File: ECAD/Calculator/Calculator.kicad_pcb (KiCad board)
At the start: 2 copper layers, 26 x 49 mm, 30 parts, among them SW1 Switch_Tactile_ESwitch, SW10 Switch_Tactile_ESwitch, SW11 Switch_Tactile_ESwitch, SW12 Switch_Tactile_ESwitch, SW13 Switch_Tactile_ESwitch, SW14 Switch_Tactile_ESwitch, SW15 Switch_Tactile_ESwitch, SW16 Switch_Tactile_ESwitch, SW17 Switch_Tactile_ESwitch, SW18 Switch_Tactile_ESwitch, SW19 Switch_Tactile_ESwitch, SW2 Switch_Tactile_ESwitch, SW20 Switch_Tactile_ESwitch, SW3 Switch_Tactile_ESwitch, SW4 Switch_Tactile_ESwitch, SW5 Switch_Tactile_ESwitch, SW6 Switch_Tactile_ESwitch, SW7 Switch_Tactile_ESwitch, SW8 Switch_Tactile_ESwitch, SW9 Switch_Tactile_ESwitch

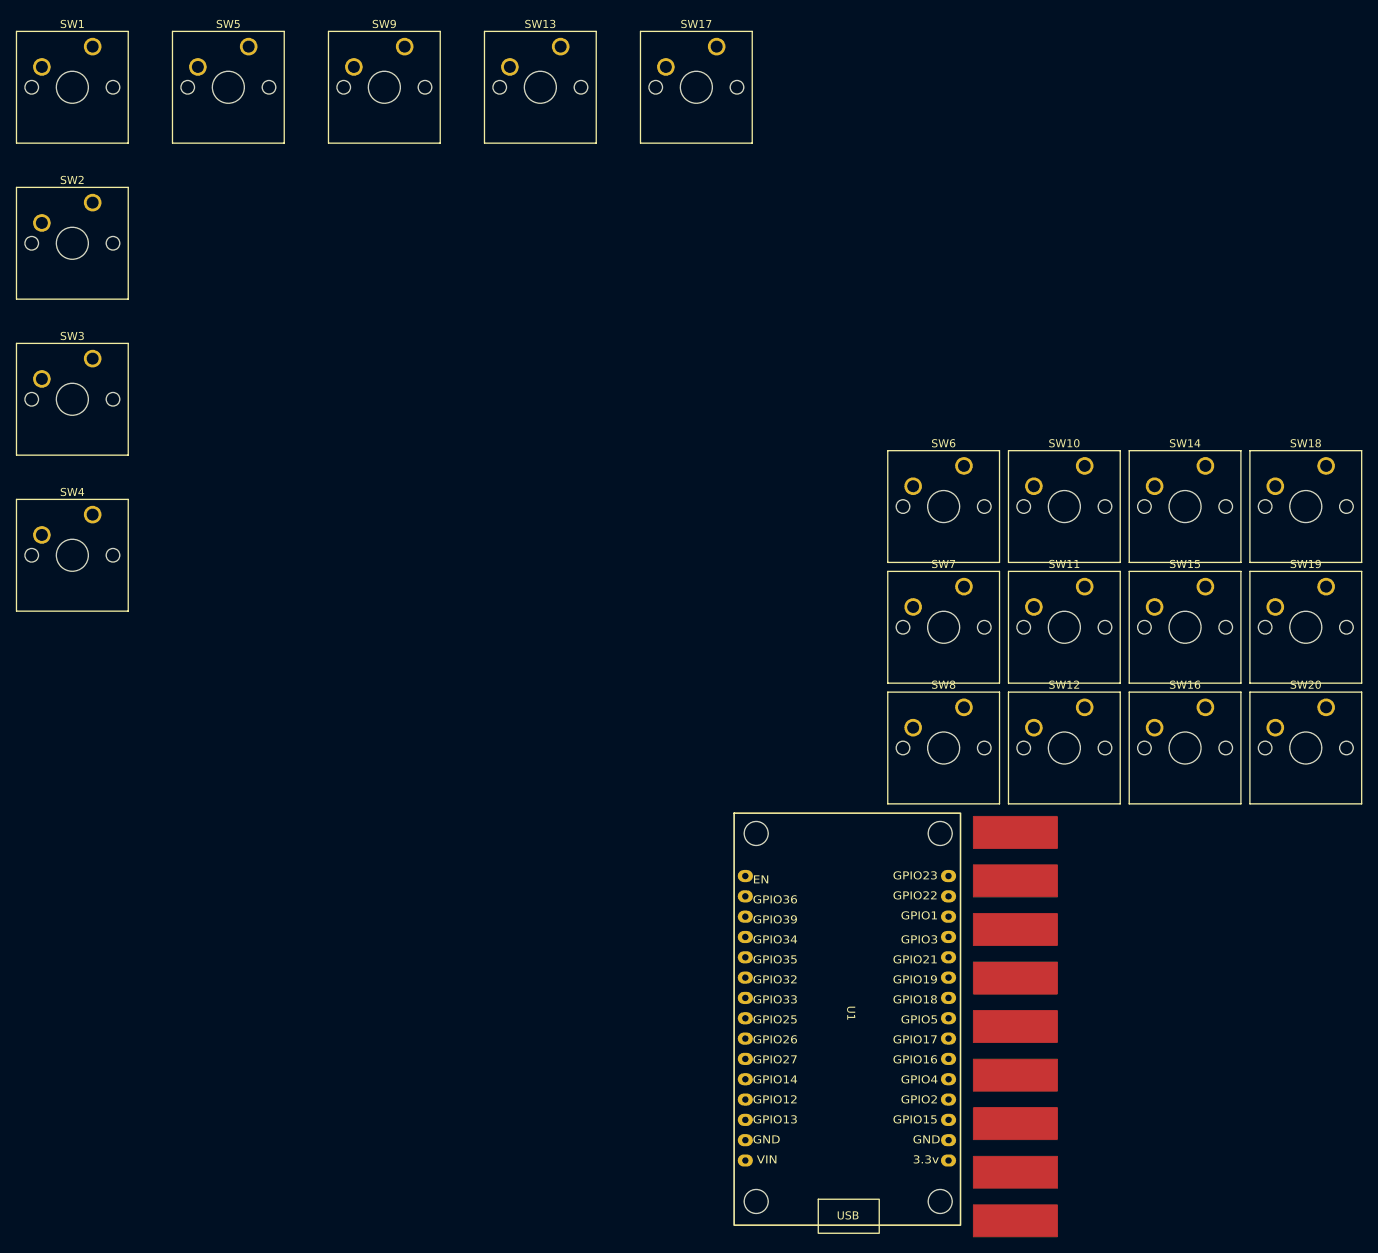
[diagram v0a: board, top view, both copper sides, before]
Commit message: Completed layout for footprints for PCB
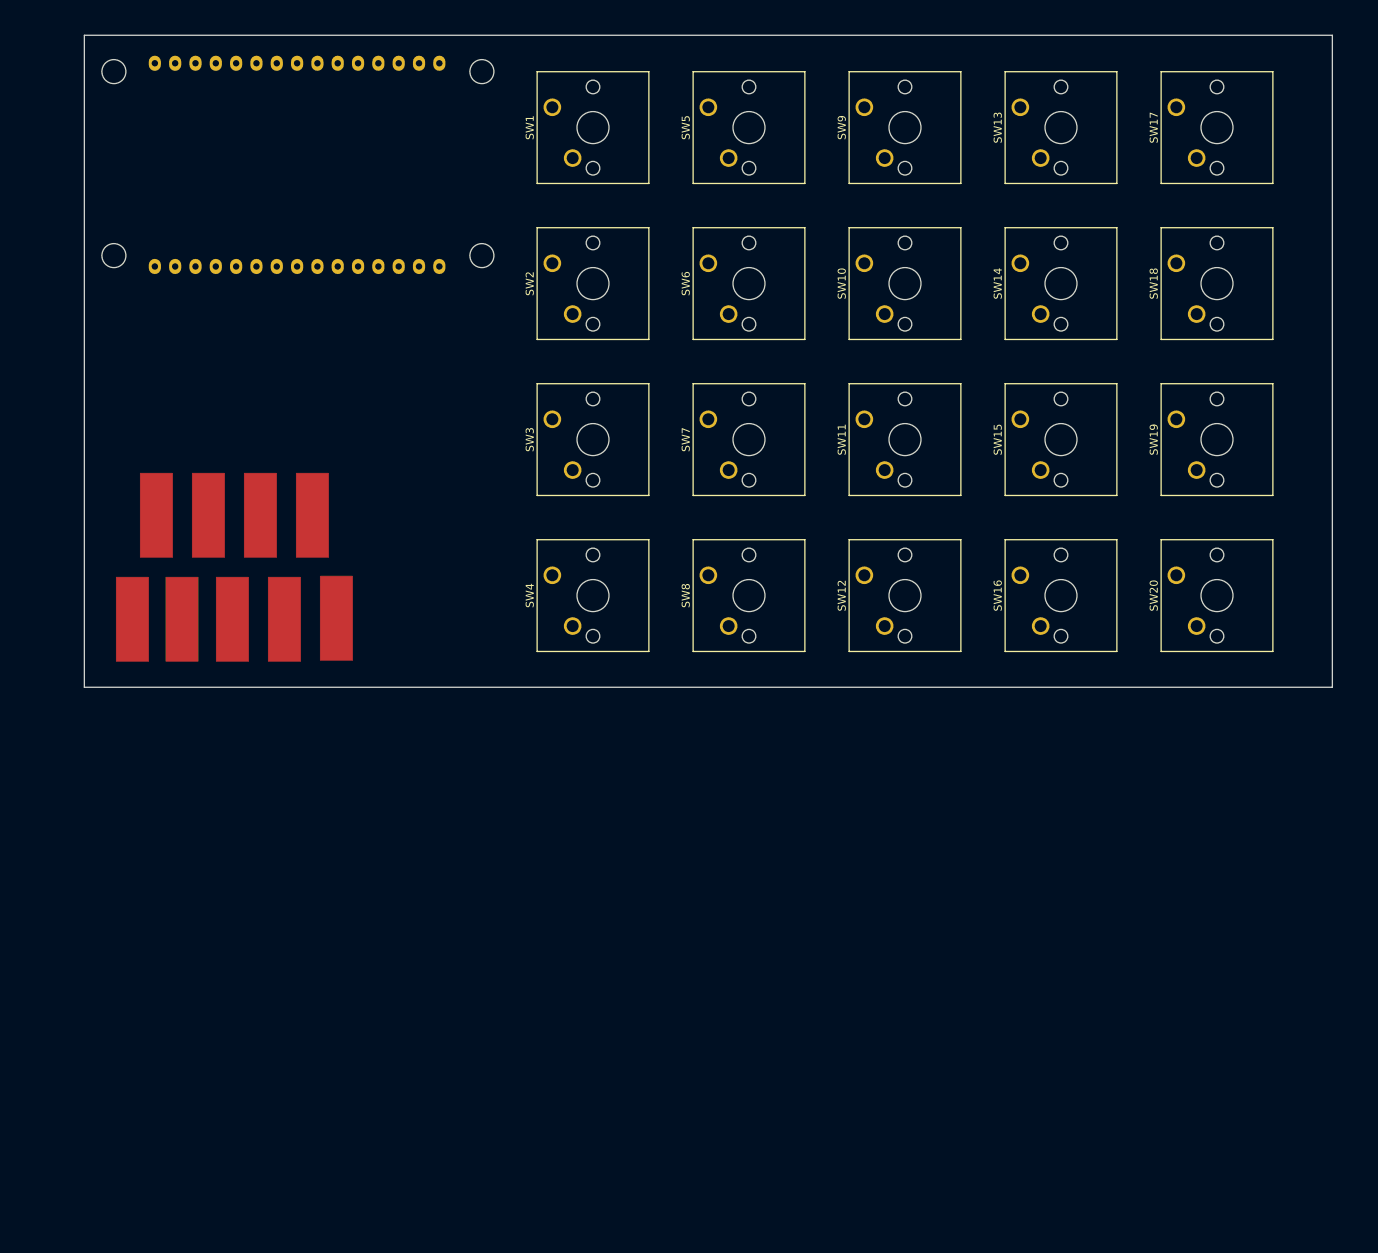
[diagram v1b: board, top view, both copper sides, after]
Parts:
- U1: moved to B.Cu
- moved TP9 133.6 mm to (32.0, 91.0), turned to 90 degrees
- moved U1 126.9 mm to (51.8, 35.0), turned to 90 degrees
- moved TP7 116.2 mm to (54.5, 78.0), turned to 90 degrees
- moved TP1 114.5 mm to (35.0, 78.0), turned to 90 degrees
- moved TP5 114.0 mm to (48.0, 78.0), turned to 90 degrees
- moved TP3 113.4 mm to (41.5, 78.0), turned to 90 degrees
- moved TP8 109.5 mm to (57.5, 90.9), turned to 90 degrees
- moved TP2 109.2 mm to (38.2, 91.0), turned to 90 degrees
- moved TP6 107.7 mm to (51.0, 91.0), turned to 90 degrees
- moved TP4 107.7 mm to (44.5, 91.0), turned to 90 degrees
- moved SW1 58.0 mm to (84.5, 27.0), turned to 90 degrees
- moved SW2 58.0 mm to (84.5, 46.5), turned to 90 degrees
- moved SW3 58.0 mm to (84.5, 66.0), turned to 90 degrees
- moved SW4 58.0 mm to (84.5, 85.5), turned to 90 degrees
- moved SW5 58.0 mm to (104.0, 27.0), turned to 90 degrees
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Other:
- board size 26 x 49 mm -> 156 x 81.5 mm

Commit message: Update PCB layout and added vias across the PCB
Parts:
- moved TP9 0.50 mm to (31.5, 91.0)
- moved TP2 0.20 mm to (38.0, 91.0)
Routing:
- net (no net): track 0.00 -> 136.9 mm, vias 0 -> 18
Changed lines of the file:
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@@
 	(footprint "Calculator_lib:Solder_pad"
 		(layer "F.Cu")
-		(at 32 91 90)
+		(at 31.5 91 90)
 		(property "Reference" "TP9"
 			(at 0 -0.5 90)
@@
 		)
 		(property "Value" "TestPoint"
-			(at 0 -3.5 90)
+			(at 0 -3 90)
 			(unlocked yes)
 			(layer "F.Fab")
@@
 			(polygon
 				(pts
-					(xy 29.50013 96.750038) (xy 29.5 85.25) (xy 34.569861 85.280882) (xy 34.5 96.75)
+					(xy 29.00013 96.750038) (xy 29 85.25) (xy 34.069861 85.280882) (xy 34 96.75)
 				)
 			)
@@
 		)
 		(property "Value" "TestPoint"
-			(at 0 -3.5 90)
+			(at 0 -3 90)
 			(unlocked yes)
 			(layer "F.Fab")
@@
 		)
 		(property "Value" "TestPoint"
-			(at 0 -3.5 90)
+			(at 0 -3 90)
 			(unlocked yes)
 			(layer "F.Fab")
@@
 		)
 		(property "Value" "TestPoint"
-			(at 0 -3.5 90)
+			(at 0 -3 90)
 			(unlocked yes)
 			(layer "F.Fab")
@@
 		)
 		(property "Value" "TestPoint"
-			(at 0 -3.5 90)
+			(at 0 -3 90)
 			(unlocked yes)
 			(layer "F.Fab")
@@
 		)
 		(property "Value" "TestPoint"
-			(at 0 -3.5 90)
+			(at 0 -3 90)
 			(unlocked yes)
 			(layer "F.Fab")
@@
 	(footprint "Calculator_lib:Solder_pad"
 		(layer "F.Cu")
-		(at 38.204861 91 90)
+		(at 38 91 90)
 		(property "Reference" "TP2"
 			(at 0 -0.5 90)
@@
 		)
 		(property "Value" "TestPoint"
-			(at 0 -3.5 90)
+			(at 0 -3.204861 90)
 			(unlocked yes)
 			(layer "F.Fab")
@@
 			(polygon
 				(pts
-					(xy 35.704991 96.750038) (xy 35.704861 85.25) (xy 40.774722 85.280882) (xy 40.704861 96.75)
+					(xy 35.50013 96.750038) (xy 35.5 85.25) (xy 40.569861 85.280882) (xy 40.5 96.75)
 				)
 			)
@@
 		)
 		(property "Value" "TestPoint"
-			(at 0 -3.5 90)
+			(at 0 -3 90)
 			(unlocked yes)
 			(layer "F.Fab")
@@
 		)
 		(property "Value" "TestPoint"
-			(at 0 -3.5 90)
+			(at 0 -3 90)
 			(unlocked yes)
 			(layer "F.Fab")
@@
 		(layer "Edge.Cuts")
 	)
+	(segment
+		(start 44.5 91)
+		(end 44.5 70)
+		(width 0.2)
+		(layer "F.Cu")
+		(net "")
+	)
+	(segment
+		(start 51 91)
+		(end 51 70)
+		(width 0.2)
+		(layer "F.Cu")
+		(net "")
+	)
+	(segment
+		(start 35 78)
+		(end 35 70)
+		(width 0.2)
+		(layer "F.Cu")
+		(net "")
+	)
+	(segment
+		(start 38 91)
+		(end 38 70)
+		(width 0.2)
+		(layer "F.Cu")
+		(net "")
+	)
+	(segment
+		(start 31.5 91)
+		(end 31.5 70)
+		(width 0.2)
+		(layer "F.Cu")
+		(net "")
+	)
+	(segment
+		(start 48 78)
+		(end 48 70)
+		(width 0.2)
+		(layer "F.Cu")
+		(net "")
+	)
+	(segment
+		(start 57.5 90.870014)
+		(end 57.5 70)
+		(width 0.2)
+		(layer "F.Cu")
+		(net "")
+	)
+	(segment
+		(start 54.5 78)
+		(end 54.5 70)
+		(width 0.2)
+		(layer "F.Cu")
+		(net "")
+	)
+	(segment
+		(start 41.5 78)
+		(end 41.5 70)
+		(width 0.2)
+		(layer "F.Cu")
+		(net "")
+	)
+	(via
+		(at 143 21)
+		(size 0.6)
+		(drill 0.3)
+		(layers "F.Cu" "B.Cu")
+		(net "")
+	)
+	(via
+		(at 84.5 21)
+		(size 0.6)
+		(drill 0.3)
+		(layers "F.Cu" "B.Cu")
+		(net "")
+	)
+	(via
+		(at 44.5 70)
+		(size 0.6)
+		(drill 0.3)
+		(layers "F.Cu" "B.Cu")
+		(net "")
+	)
+	(via
+		(at 48 70)
+		(size 0.6)
+		(drill 0.3)
+		(layers "F.Cu" "B.Cu")
+		(net "")
+	)
+	(via
+		(at 38 70)
+		(size 0.6)
+		(drill 0.3)
+		(layers "F.Cu" "B.Cu")
+		(net "")
+	)
+	(via
+		(at 54.5 70)
+		(size 0.6)
+		(drill 0.3)
+		(layers "F.Cu" "B.Cu")
+		(net "")
+	)
+	(via
+		(at 162.5 21)
+		(size 0.6)
+		(drill 0.3)
+		(layers "F.Cu" "B.Cu")
+		(net "")
+	)
+	(via
+		(at 104 21)
+		(size 0.6)
+		(drill 0.3)
+		(layers "F.Cu" "B.Cu")
+		(net "")
+	)
+	(via
+		(at 31.5 70)
+		(size 0.6)
+		(drill 0.3)
+		(layers "F.Cu" "B.Cu")
+		(net "")
+	)
+	(via
+		(at 51 70)
+		(size 0.6)
+		(drill 0.3)
+		(layers "F.Cu" "B.Cu")
+		(net "")
+	)
+	(via
+		(at 57.5 70)
+		(size 0.6)
+		(drill 0.3)
+		(layers "F.Cu" "B.Cu")
+		(net "")
+	)
+	(via
+		(at 41.5 70)
+		(size 0.6)
+		(drill 0.3)
+		(layers "F.Cu" "B.Cu")
+		(net "")
+	)
+	(via
+		(at 79 85.5)
+		(size 0.6)
+		(drill 0.3)
+		(layers "F.Cu" "B.Cu")
+		(net "")
+	)
+	(via
+		(at 79 46.5)
+		(size 0.6)
+		(drill 0.3)
+		(layers "F.Cu" "B.Cu")
+		(net "")
+	)
+	(via
+		(at 79 66)
+		(size 0.6)
+		(drill 0.3)
+		(layers "F.Cu" "B.Cu")
+		(net "")
+	)
+	(via
+		(at 79 27)
+		(size 0.6)
+		(drill 0.3)
+		(layers "F.Cu" "B.Cu")
+		(net "")
+	)
+	(via
+		(at 35 70)
+		(size 0.6)
+		(drill 0.3)
+		(layers "F.Cu" "B.Cu")
+		(net "")
+	)
+	(via
+		(at 123.5 21)
+		(size 0.6)
+		(drill 0.3)
+		(layers "F.Cu" "B.Cu")
+		(net "")
+	)
 	(embedded_fonts no)

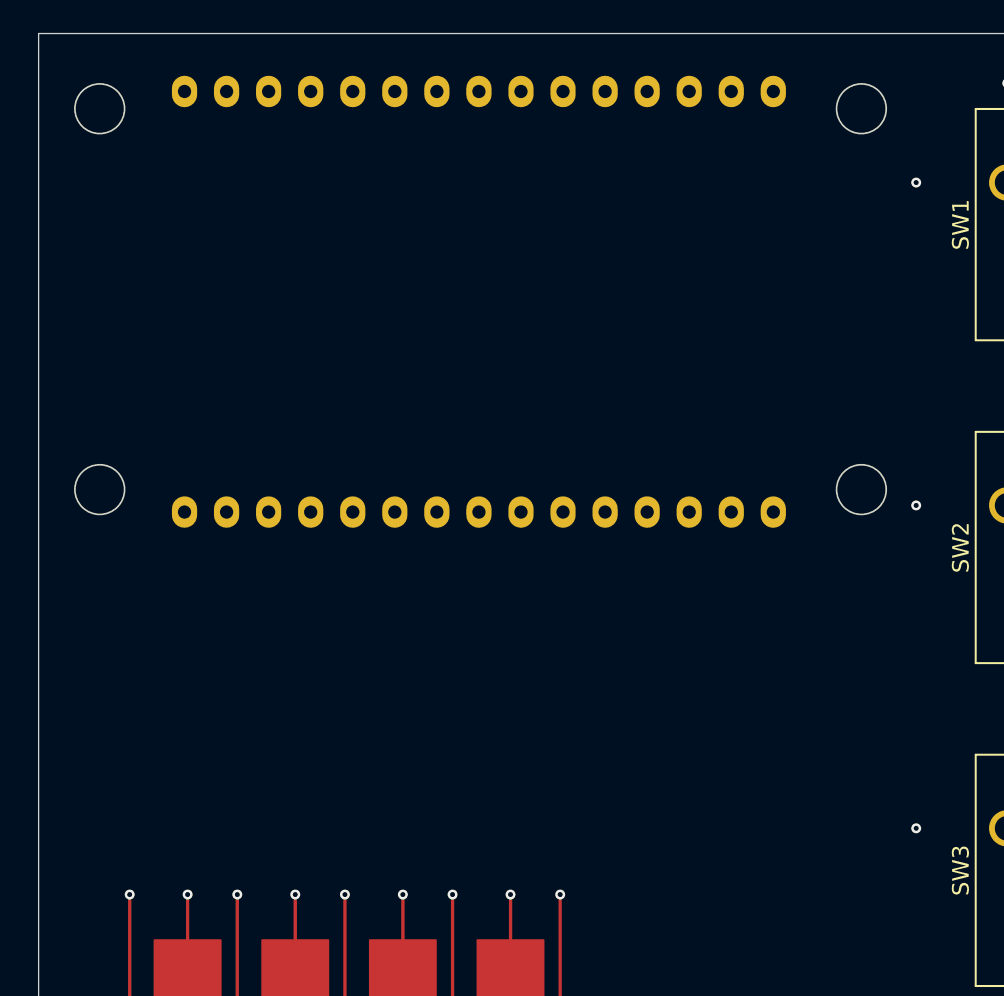
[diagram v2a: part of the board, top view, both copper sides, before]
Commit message: Connect PCB pads to ESP32 and refined form factor
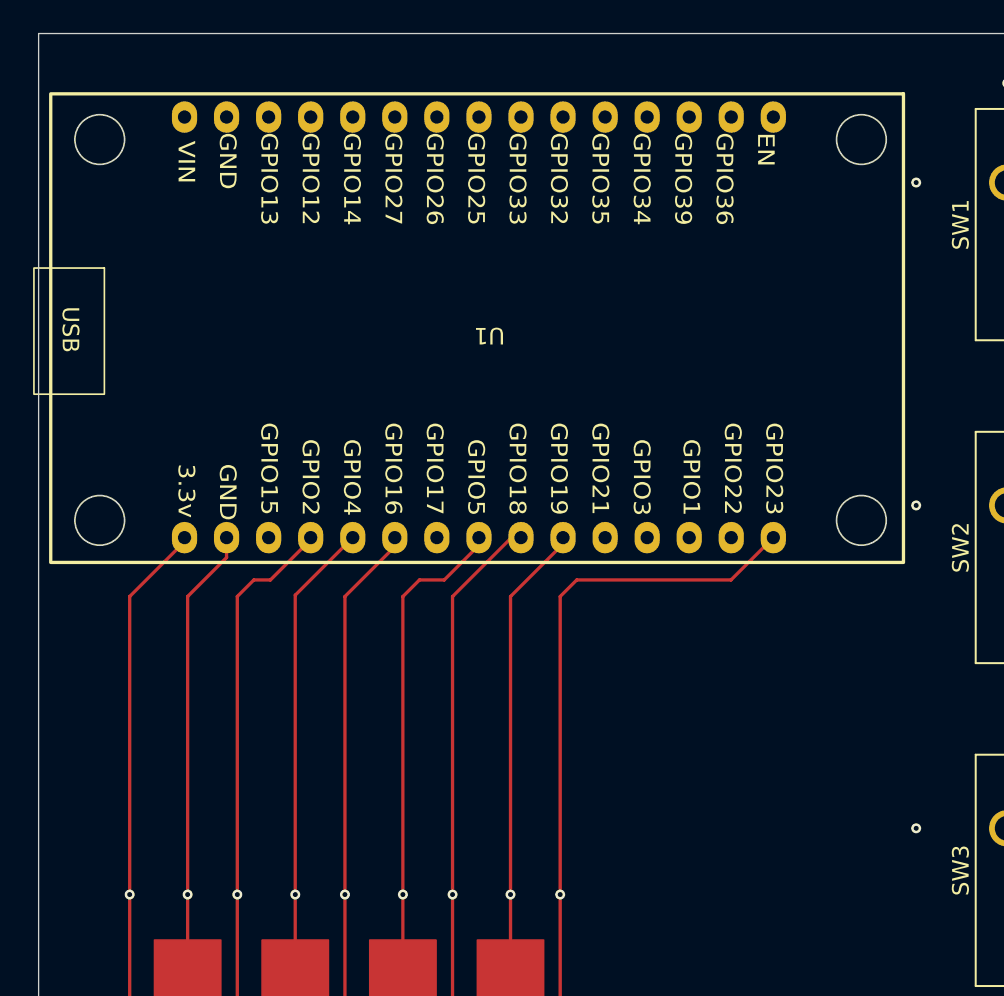
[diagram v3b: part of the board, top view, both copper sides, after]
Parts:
- U1: moved to F.Cu
- turned U1 to -90 degrees
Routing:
- net (no net): track 136.9 -> 0.00 mm, vias 18 -> 9
- net /SDI(MOSI): track 0.00 -> 53.2 mm, vias 0 -> 1
- net /DC/RS: track 0.00 -> 45.0 mm, vias 0 -> 1
- net /SCK: track 0.00 -> 44.6 mm, vias 0 -> 1
- net /VCC: track 0.00 -> 43.9 mm, vias 0 -> 1
- net /RESET: track 0.00 -> 43.8 mm, vias 0 -> 1
- net /CS: track 0.00 -> 32.3 mm, vias 0 -> 1
- net /LED: track 0.00 -> 31.0 mm, vias 0 -> 1
- net /SDO(MISO): track 0.00 -> 30.9 mm, vias 0 -> 1
- net /GND: track 0.00 -> 30.5 mm, vias 0 -> 1
